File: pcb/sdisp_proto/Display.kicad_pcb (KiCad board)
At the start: 2 copper layers, 85 x 28 mm, 15 parts, among them P1 CONN_02X05, U1 74HC595

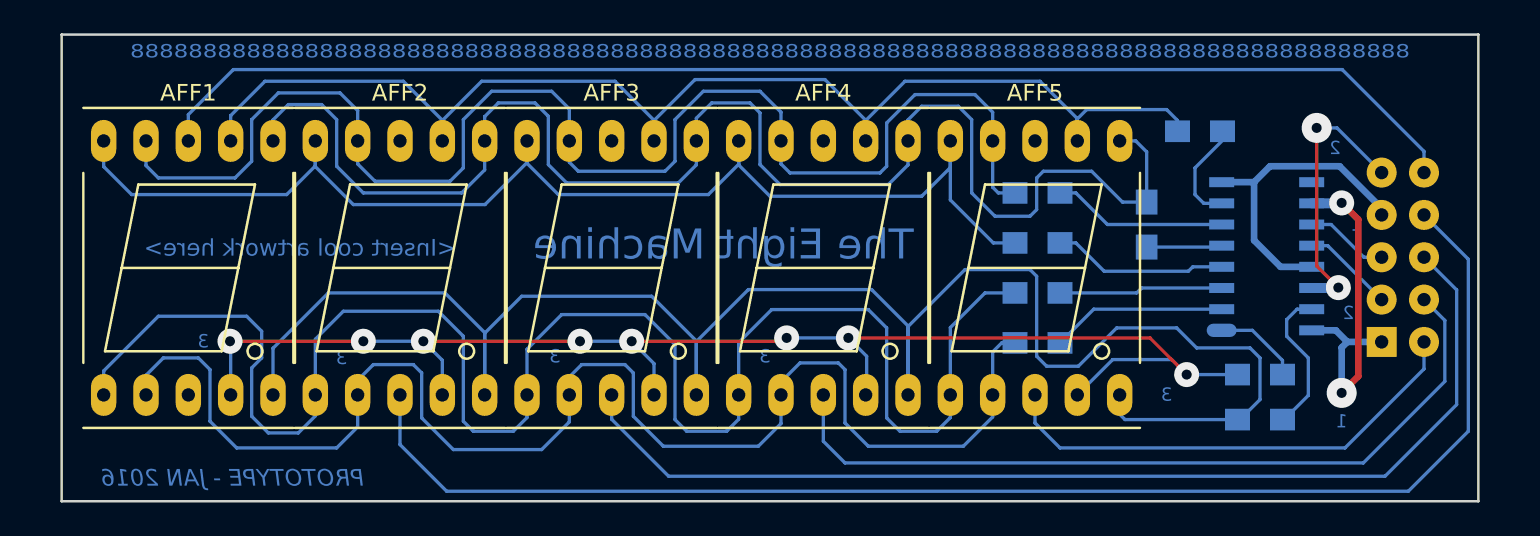
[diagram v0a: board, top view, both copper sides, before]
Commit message: Fix: Layout of the pin header on the prototype
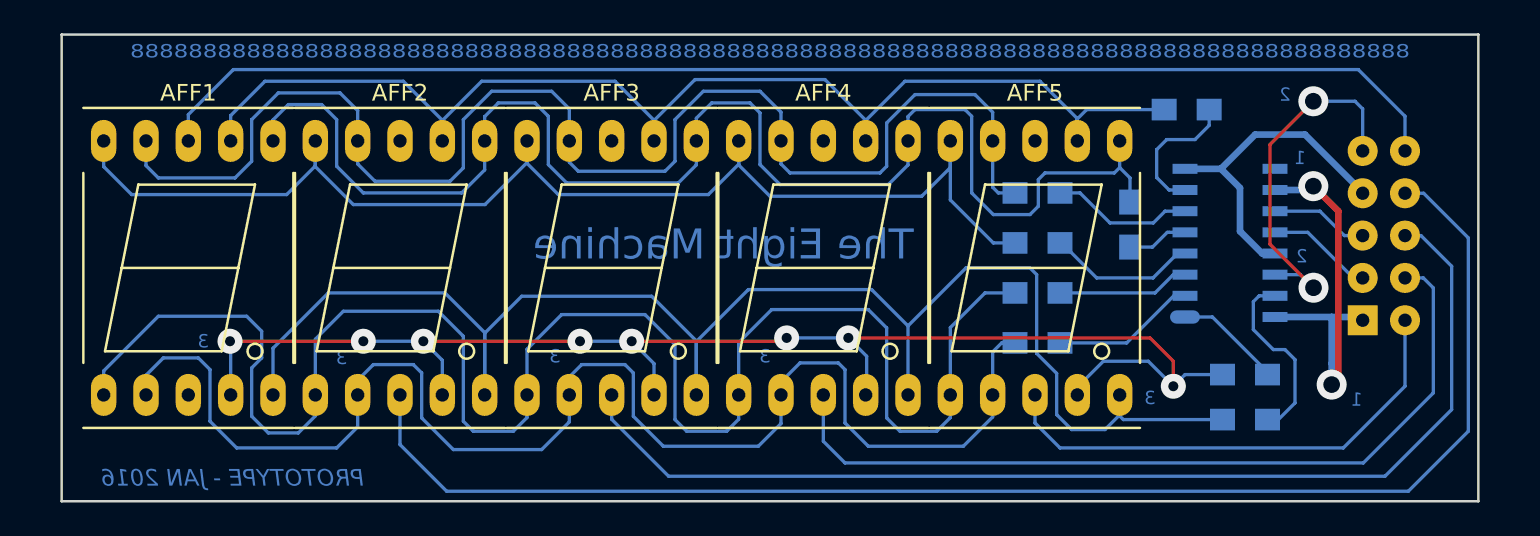
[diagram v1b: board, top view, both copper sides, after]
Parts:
- moved U1 2.34 mm to (180.7, 102.1)
- moved P1 1.73 mm to (188.7, 106.7)
- moved R1 1.53 mm to (178.1, 94.1)
- moved R2 1.00 mm to (174.7, 101.0)
- moved R3 0.90 mm to (181.6, 110.0)
- moved R8 0.90 mm to (181.6, 112.7)
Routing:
- net Net-(AFF1-Pad5): track 111.8 -> 96.5 mm
- net Data: track 16.7 -> 21.7 mm
- net Net-(AFF1-Pad6): track 89.9 -> 86.5 mm
- net VCC: track 21.7 -> 24.5 mm
- net D1: track 83.8 -> 86.2 mm
- net D2: track 65.0 -> 67.1 mm
- net A: track 6.30 -> 8.39 mm
- net DP: track 9.00 -> 11.0 mm
- net F: track 10.5 -> 8.54 mm
- net D: track 10.5 -> 8.67 mm
- net E: track 9.82 -> 7.95 mm
- net D3: track 48.1 -> 49.9 mm
- net Net-(AFF1-Pad7): track 76.2 -> 74.5 mm
- net G: track 10.5 -> 8.98 mm
- net D0: track 80.1 -> 78.9 mm
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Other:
- net class Default: via_dia 1.2 -> 1.8; via_drill 0.8 -> 1
- board text removed: "<Insert cool artwork here>"
